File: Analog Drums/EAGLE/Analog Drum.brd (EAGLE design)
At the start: 100 x 50 mm, 78 parts, among them IC1 LM741P, IC2 LM741P, IC3 LM741P, IC4 LM741P, IC5 LM741P, Q1 2N3906, Q2 2N3906, T2 2N3904, T3 2N3904, T4 2N3904

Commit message: I think im done
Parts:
- C13: value 40n -> 47n
- moved R30 90.1 mm to (8.00, 48.0), turned to 180 degrees
- moved R25 1.00 mm to (62.0, 37.0)
- moved R36 1.00 mm to (58.0, 37.0)
- turned C22 to 180 degrees
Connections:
- removed net POT2_3: T4.1
- net POT1: now also T4.1
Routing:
- net POT5: track 0.00 -> 78.9 mm, vias 0 -> 2
- net POT6_7: track 0.00 -> 73.4 mm, vias 0 -> 2
- net POT4: track 5.14 -> 75.5 mm, vias 0 -> 5
- net POT8: track 0.00 -> 58.0 mm, vias 0 -> 3
- net RES_TRIG: track 20.5 -> 78.3 mm, vias 0 -> 6
- net POT3: track 15.7 -> 67.1 mm, vias 0 -> 3
- net BUFFERED: track 12.4 -> 59.0 mm
- net POT9: track 12.5 -> 58.4 mm
- net RES_FTR_COM: track 35.3 -> 79.0 mm, vias 1 -> 3
- net POT1: track 6.45 -> 49.7 mm, vias 0 -> 2
- net N$12: track 14.9 -> 47.7 mm
- net -12V: track 192.2 -> 220.1 mm, vias 0 -> 1
- net +12V: track 32.6 -> 55.9 mm, vias 13 -> 27
- net N$29: track 0.00 -> 21.6 mm
- net N$9: track 2.42 -> 23.1 mm
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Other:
- board text added: "+12V"
- board text added: "-12V"
- board text added: "0V"
- board text added: "Drum - Generic Feb 2019 Koltin Kosik-Harvey"
- board text added: "OUT"
- board text added: "TRIG"

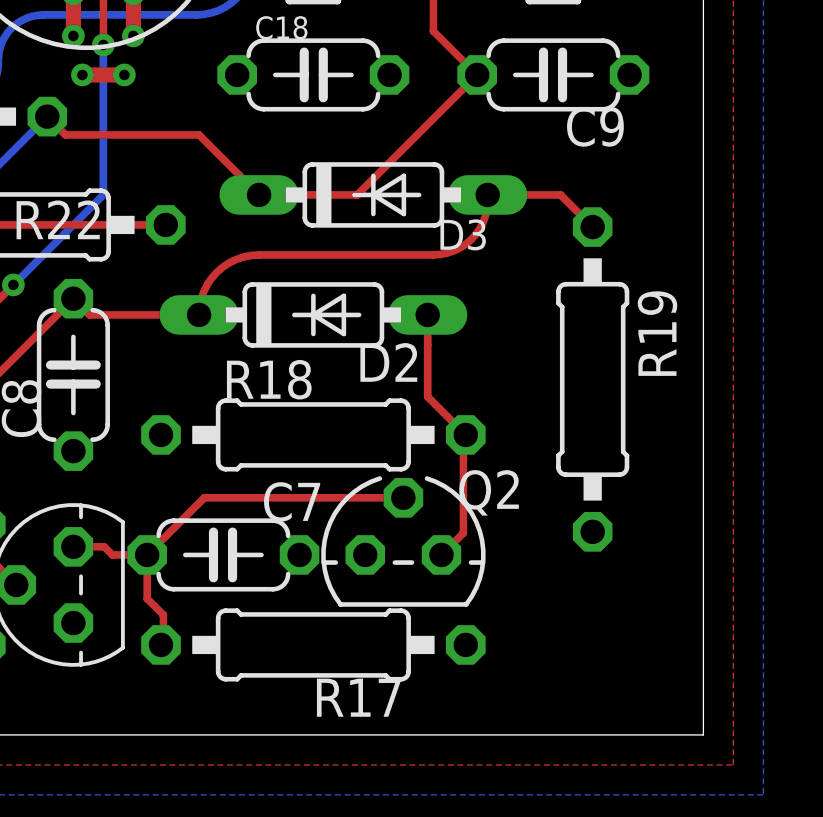
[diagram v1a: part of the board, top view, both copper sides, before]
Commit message: Added 100ohm resistor
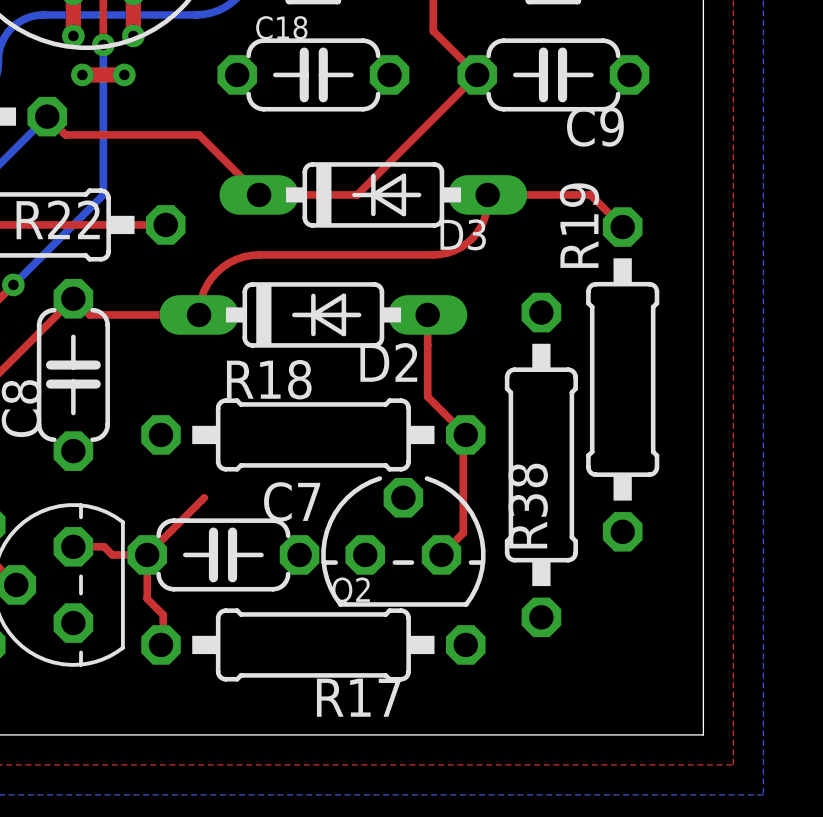
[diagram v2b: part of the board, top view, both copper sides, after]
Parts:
- added R38: 100, resistor:0207/10
- moved R19 1.00 mm to (97.3, 11.8)
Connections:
- new net N$5: Q2.2, R38.1
- net N$14: now also R38.2; no longer Q2.2
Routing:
- net N$14: track 15.2 -> 8.52 mm
- net N$16: track 26.9 -> 27.9 mm
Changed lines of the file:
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@@
 <?xml version="1.0" encoding="utf-8"?>
 <!DOCTYPE eagle SYSTEM "eagle.dtd">
-<eagle version="9.2.2">
+<eagle version="9.3.1">
 <drawing>
 <settings>
@@
 </element>
 <element name="Q2" library="transistor-pnp" library_urn="urn:adsk.eagle:library:399" package="TO92" package3d_urn="urn:adsk.eagle:package:29211/2" value="2N3906" x="90" y="6" smashed="yes">
-<attribute name="NAME" x="91.775" y="7.535" size="1.27" layer="25" ratio="10"/>
-<attribute name="VALUE" x="92.375" y="4.23" size="1.27" layer="27" ratio="10"/>
+<attribute name="NAME" x="87.575" y="4.435" size="0.8" layer="25" ratio="10"/>
+<attribute name="VALUE" x="89.675" y="4.43" size="0.8" layer="27" ratio="10"/>
 </element>
 <element name="R10" library="resistor" library_urn="urn:adsk.eagle:library:348" package="0207/10" package3d_urn="urn:adsk.eagle:package:25939/1" value="10k" x="15" y="31" smashed="yes" rot="R90">
@@
 <attribute name="VALUE" x="89.2606" y="10.635" size="1.27" layer="27" ratio="10" rot="R180"/>
 </element>
-<element name="R19" library="resistor" library_urn="urn:adsk.eagle:library:348" package="0207/10" package3d_urn="urn:adsk.eagle:package:25939/1" value="10k" x="96.31" y="11.85" smashed="yes" rot="R270">
-<attribute name="NAME" x="97.834" y="14.898" size="1.27" layer="25" ratio="10" rot="R270"/>
-<attribute name="VALUE" x="95.675" y="14.1106" size="1.27" layer="27" ratio="10" rot="R270"/>
+<element name="R19" library="resistor" library_urn="urn:adsk.eagle:library:348" package="0207/10" package3d_urn="urn:adsk.eagle:package:25939/1" value="10k" x="97.31" y="11.85" smashed="yes" rot="R270">
+<attribute name="NAME" x="95.234" y="18.498" size="1.27" layer="25" ratio="10" rot="R270"/>
+<attribute name="VALUE" x="96.675" y="14.1106" size="1.27" layer="27" ratio="10" rot="R270"/>
 </element>
 <element name="R21" library="resistor" library_urn="urn:adsk.eagle:library:348" package="0207/10" package3d_urn="urn:adsk.eagle:package:25939/1" value="47k" x="73.05" y="20.61" smashed="yes" rot="R180">
@@
 <attribute name="NAME" x="70.841" y="31.597" size="1.27" layer="25" ratio="10"/>
 <attribute name="VALUE" x="69.841" y="29.033" size="1.27" layer="27" ratio="10"/>
+</element>
+<element name="R38" library="resistor" library_urn="urn:adsk.eagle:library:348" package="0207/10" package3d_urn="urn:adsk.eagle:package:25939/1" value="100" x="94.6" y="9" smashed="yes" rot="R270">
+<attribute name="NAME" x="93.524" y="9.148" size="1.27" layer="25" ratio="10" rot="R270"/>
+<attribute name="VALUE" x="94.265" y="12.1606" size="1.27" layer="27" ratio="10" rot="R270"/>
 </element>
 </elements>
@@
 <contactref element="T3" pad="1"/>
 <contactref element="C7" pad="2"/>
-<contactref element="Q2" pad="2"/>
 <wire x1="79" y1="6.27" x2="80.03" y2="6.27" width="0.254" layer="1"/>
 <wire x1="80.3" y1="6" x2="81.46" y2="6" width="0.254" layer="1"/>
@@
 <wire x1="82" y1="3.08" x2="81.92" y2="3" width="0.254" layer="1"/>
 <wire x1="81.46" y1="6" x2="83.365" y2="7.905" width="0.254" layer="1"/>
-<wire x1="83.365" y1="7.905" x2="90" y2="7.905" width="0.254" layer="1"/>
+<contactref element="R38" pad="2"/>
+<wire x1="94.6" y1="3.92" x2="79" y2="6.27" width="0" layer="19" extent="1-1"/>
 </signal>
 <signal name="N$15">
@@
 <contactref element="D3" pad="A"/>
 <contactref element="C10" pad="1"/>
-<wire x1="96.31" y1="16.93" x2="95.24" y2="18" width="0.254" layer="1"/>
-<wire x1="95.24" y1="18" x2="92.81" y2="18" width="0.254" layer="1"/>
+<wire x1="97.31" y1="16.93" x2="96.24" y2="18" width="0.254" layer="1"/>
+<wire x1="96.24" y1="18" x2="92.81" y2="18" width="0.254" layer="1"/>
 <wire x1="79" y1="14.54" x2="79.54" y2="14" width="0.254" layer="1"/>
 <wire x1="79.54" y1="14" x2="83.19" y2="14" width="0.254" layer="1"/>
@@
 <wire x1="13.08" y1="42.84" x2="19.19" y2="36.73" width="0.254" layer="1"/>
 </signal>
+<signal name="N$5">
+<contactref element="Q2" pad="2"/>
+<contactref element="R38" pad="1"/>
+<wire x1="94.6" y1="14.08" x2="90" y2="7.905" width="0" layer="19" extent="1-1"/>
+</signal>
 </signals>

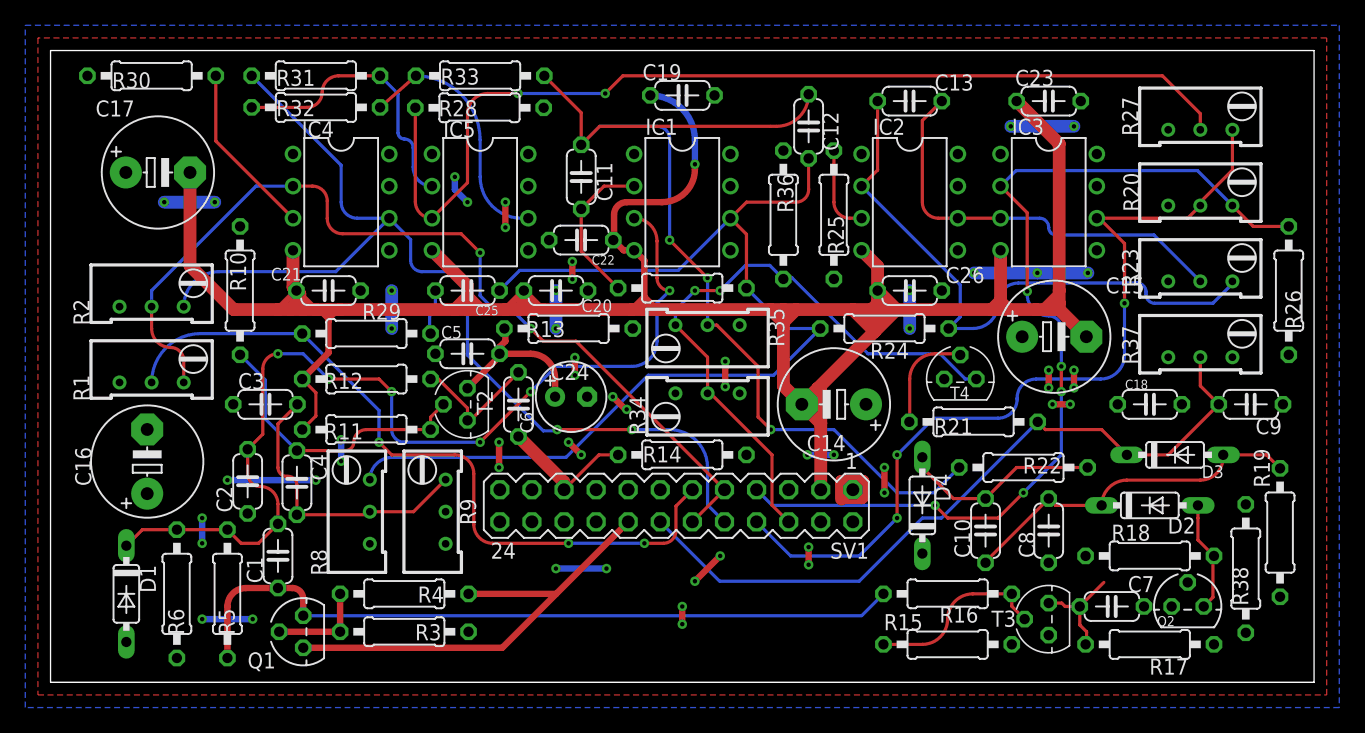
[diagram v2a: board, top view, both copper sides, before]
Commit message: Attached traces to resistor and created gerbers
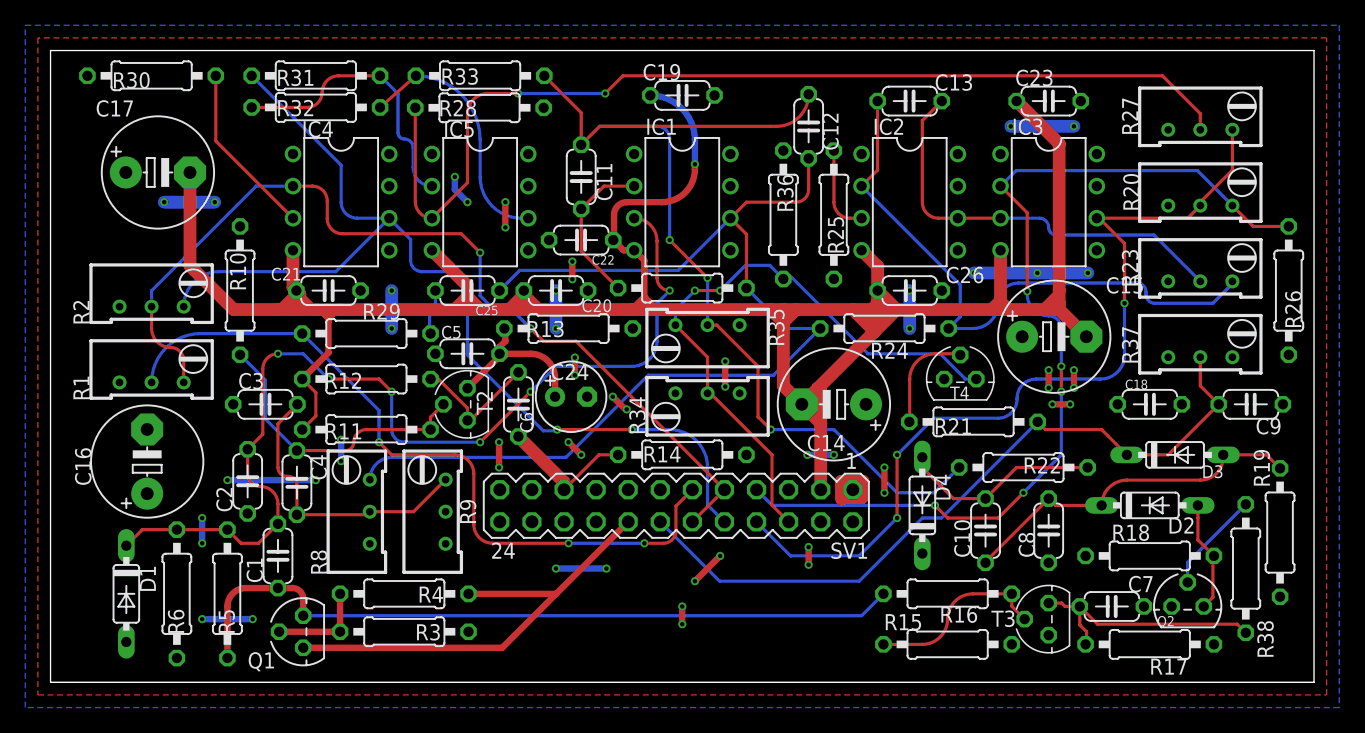
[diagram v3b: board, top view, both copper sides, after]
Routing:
- net N$14: track 8.52 -> 19.8 mm
- net N$5: track 0.00 -> 8.08 mm
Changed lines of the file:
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@@
 <?xml version="1.0" encoding="utf-8"?>
 <!DOCTYPE eagle SYSTEM "eagle.dtd">
-<eagle version="9.3.1">
+<eagle version="9.2.2">
 <drawing>
 <settings>
@@
 </class>
 </classes>
-<designrules name="default">
+<designrules name="SeeedStudio_2layer_DRU_no_angle_20140221">
 <description language="de">&lt;b&gt;EAGLE Design Rules&lt;/b&gt;
 &lt;p&gt;
@@
 necessary adjustments and save your customized
 design rules under a new name.</description>
+<description language="zh">&lt;b&gt;Seeed Studio EAGLE Design Rules&lt;/b&gt;
+</description>
 <param name="layerSetup" value="(1*16)"/>
-<param name="mtCopper" value="0.035mm 0.035mm 0.035mm 0.035mm 0.035mm 0.035mm 0.035mm 0.035mm 0.035mm 0.035mm 0.035mm 0.035mm 0.035mm 0.035mm 0.035mm 0.035mm"/>
-<param name="mtIsolate" value="1.5mm 0.15mm 0.2mm 0.15mm 0.2mm 0.15mm 0.2mm 0.15mm 0.2mm 0.15mm 0.2mm 0.15mm 0.2mm 0.15mm 0.2mm"/>
+<param name="mtCopper" value="0.035mm 0.0175mm 0.035mm 0.035mm 0.035mm 0.035mm 0.035mm 0.035mm 0.035mm 0.035mm 0.035mm 0.035mm 0.035mm 0.035mm 0.0175mm 0.035mm"/>
+<param name="mtIsolate" value="1.5mm 1.1mm 0.2mm 0.15mm 0.2mm 0.15mm 0.2mm 0.15mm 0.2mm 0.15mm 0.2mm 0.15mm 0.2mm 0.15mm 0.2mm"/>
 <param name="mdWireWire" value="6mil"/>
 <param name="mdWirePad" value="6mil"/>
@@
 <param name="mdPadVia" value="6mil"/>
 <param name="mdViaVia" value="6mil"/>
-<param name="mdSmdPad" value="6mil"/>
-<param name="mdSmdVia" value="6mil"/>
-<param name="mdSmdSmd" value="6mil"/>
-<param name="mdViaViaSameLayer" value="6mil"/>
+<param name="mdSmdPad" value="0mil"/>
+<param name="mdSmdVia" value="0mil"/>
+<param name="mdSmdSmd" value="0mil"/>
+<param name="mdViaViaSameLayer" value="8mil"/>
 <param name="mnLayersViaInSmd" value="2"/>
-<param name="mdCopperDimension" value="40mil"/>
-<param name="mdDrill" value="6mil"/>
+<param name="mdCopperDimension" value="10mil"/>
+<param name="mdDrill" value="10mil"/>
 <param name="mdSmdStop" value="0mil"/>
 <param name="msWidth" value="6mil"/>
-<param name="msDrill" value="0.35mm"/>
-<param name="msMicroVia" value="9.99mm"/>
+<param name="msDrill" value="12mil"/>
+<param name="msMicroVia" value="12mil"/>
 <param name="msBlindViaRatio" value="0.5"/>
 <param name="rvPadTop" value="0.25"/>
@@
 <param name="rlMinPadBottom" value="10mil"/>
 <param name="rlMaxPadBottom" value="20mil"/>
-<param name="rlMinViaOuter" value="8mil"/>
+<param name="rlMinViaOuter" value="6mil"/>
 <param name="rlMaxViaOuter" value="20mil"/>
-<param name="rlMinViaInner" value="8mil"/>
+<param name="rlMinViaInner" value="6mil"/>
 <param name="rlMaxViaInner" value="20mil"/>
 <param name="rlMinMicroViaOuter" value="4mil"/>
@@
 <param name="psTop" value="-1"/>
 <param name="psBottom" value="-1"/>
-<param name="psFirst" value="-1"/>
+<param name="psFirst" value="0"/>
 <param name="psElongationLong" value="100"/>
 <param name="psElongationOffset" value="100"/>
 <param name="mvStopFrame" value="1"/>
 <param name="mvCreamFrame" value="0"/>
-<param name="mlMinStopFrame" value="4mil"/>
-<param name="mlMaxStopFrame" value="4mil"/>
+<param name="mlMinStopFrame" value="2mil"/>
+<param name="mlMaxStopFrame" value="2mil"/>
 <param name="mlMinCreamFrame" value="0mil"/>
 <param name="mlMaxCreamFrame" value="0mil"/>
-<param name="mlViaStopLimit" value="0mil"/>
+<param name="mlViaStopLimit" value="100mil"/>
 <param name="srRoundness" value="0"/>
 <param name="srMinRoundness" value="0mil"/>
@@
 <param name="checkAngle" value="0"/>
 <param name="checkFont" value="1"/>
-<param name="checkRestrict" value="1"/>
+<param name="checkRestrict" value="0"/>
 <param name="checkStop" value="0"/>
 <param name="checkValues" value="0"/>
@@
 </element>
 <element name="R38" library="resistor" library_urn="urn:adsk.eagle:library:348" package="0207/10" package3d_urn="urn:adsk.eagle:package:25939/1" value="100" x="94.6" y="9" smashed="yes" rot="R270">
-<attribute name="NAME" x="93.524" y="9.148" size="1.27" layer="25" ratio="10" rot="R270"/>
+<attribute name="NAME" x="95.524" y="4.948" size="1.27" layer="25" ratio="10" rot="R270"/>
 <attribute name="VALUE" x="94.265" y="12.1606" size="1.27" layer="27" ratio="10" rot="R270"/>
 </element>
@@
 <wire x1="82" y1="4" x2="82" y2="3.08" width="0.254" layer="1"/>
 <wire x1="82" y1="3.08" x2="81.92" y2="3" width="0.254" layer="1"/>
-<wire x1="81.46" y1="6" x2="83.365" y2="7.905" width="0.254" layer="1"/>
 <contactref element="R38" pad="2"/>
-<wire x1="94.6" y1="3.92" x2="79" y2="6.27" width="0" layer="19" extent="1-1"/>
+<wire x1="81.46" y1="6" x2="82.86" y2="4.6" width="0.254" layer="1"/>
+<wire x1="93.92" y1="4.6" x2="94.6" y2="3.92" width="0.254" layer="1"/>
+<wire x1="82.86" y1="4.6" x2="93.92" y2="4.6" width="0.254" layer="1"/>
 </signal>
 <signal name="N$15">
@@
 <contactref element="Q2" pad="2"/>
 <contactref element="R38" pad="1"/>
-<wire x1="94.6" y1="14.08" x2="90" y2="7.905" width="0" layer="19" extent="1-1"/>
+<wire x1="94.6" y1="14.08" x2="90" y2="9.48" width="0.254" layer="16"/>
+<wire x1="90" y1="9.48" x2="90" y2="7.905" width="0.254" layer="16"/>
 </signal>
 </signals>
